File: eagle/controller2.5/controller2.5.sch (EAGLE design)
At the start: 46 parts, among them Q1 MOSFET-PCHANNELNDP6020P_20V_2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, Q2 2N2907, U1 ATMEGA328P

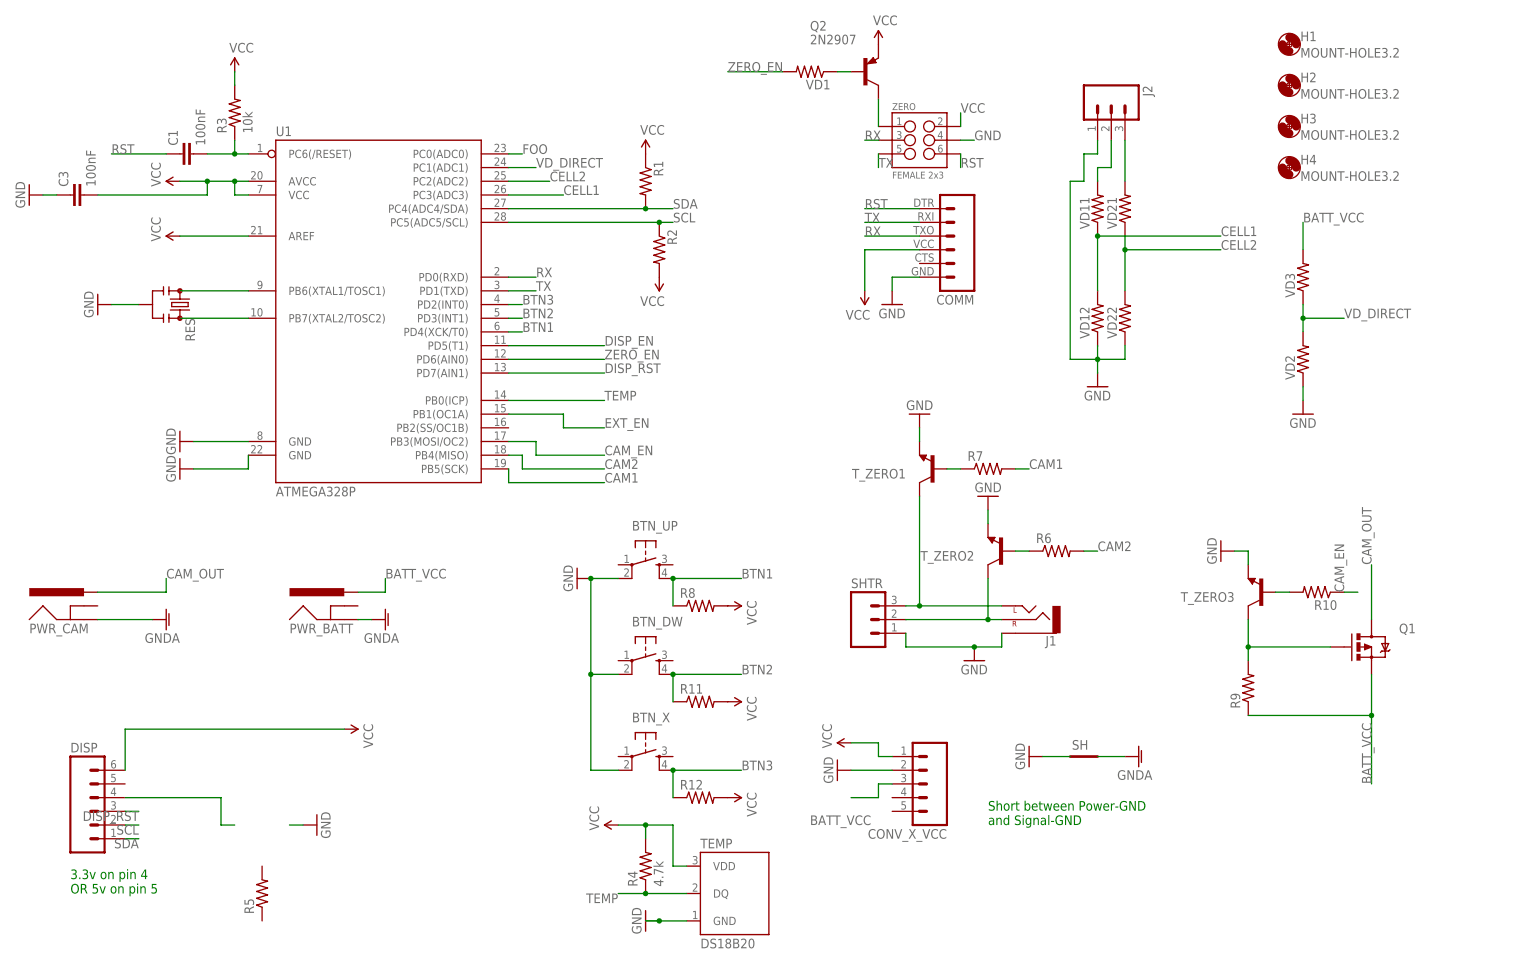
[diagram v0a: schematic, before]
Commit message: controller2.5: smaller board
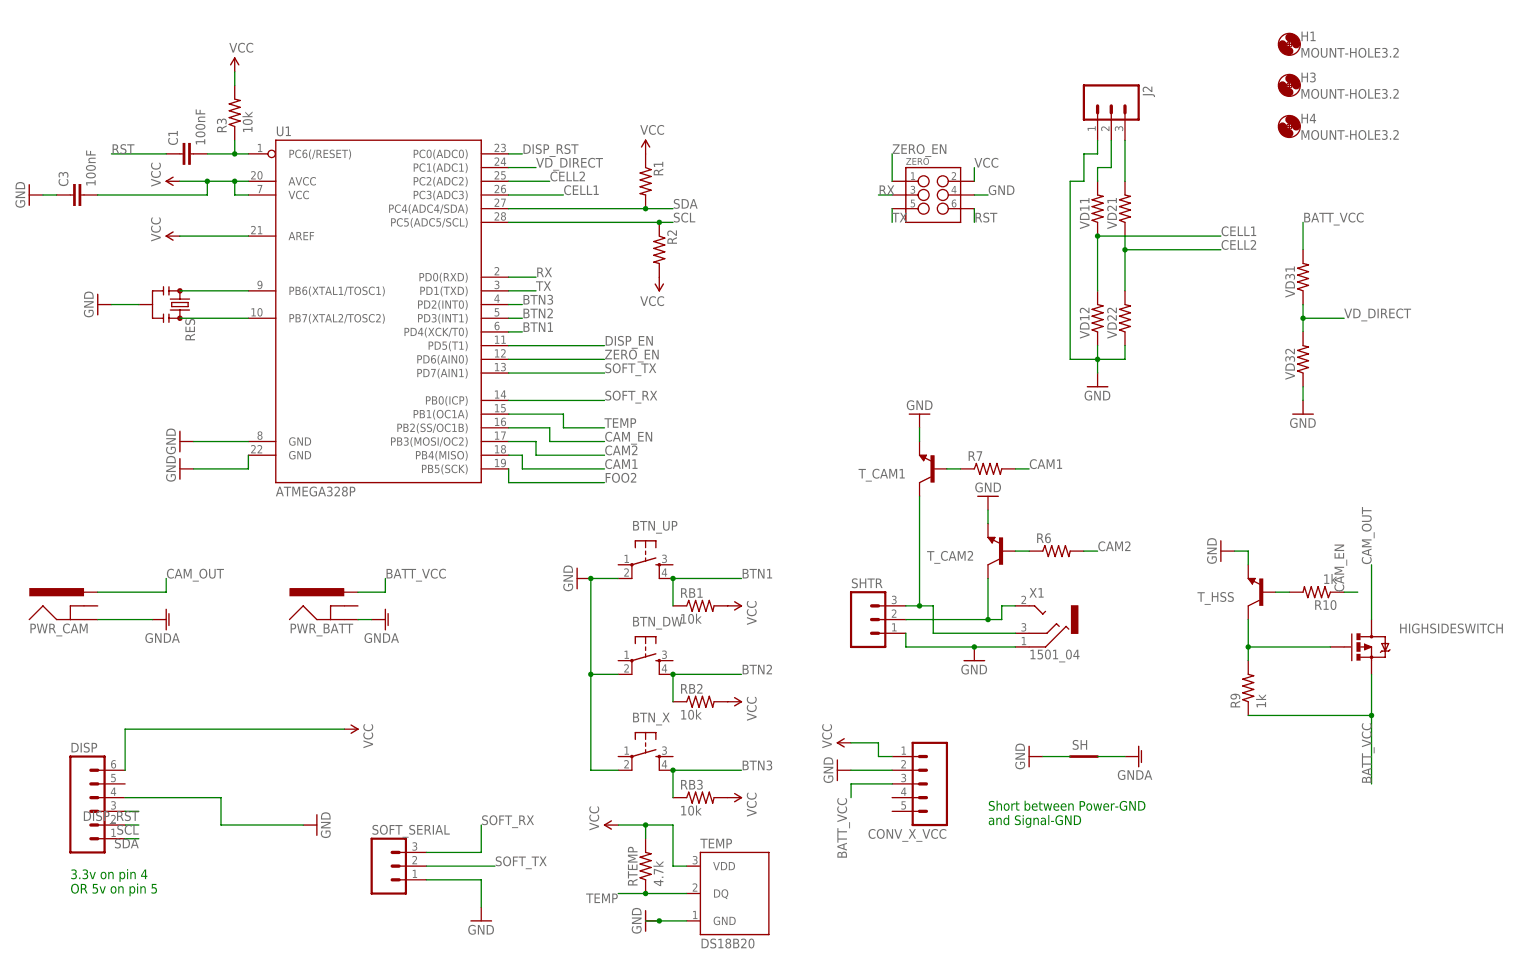
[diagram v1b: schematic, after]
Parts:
- removed COMM: FTDI_BASICPTH, SparkFun-Connectors:FTDI_BASICPTH
- removed H2: MOUNT-HOLE3.2, holes:MOUNT-HOLE3.2
- removed J1: (no value), SparkFun-Connectors:AUDIO-JACK2.5MM
- removed Q2: 2N2907, adafruit:2N2907
- removed R5, VD1: (no value), SparkFun-Resistors:RESISTORAXIAL-0.3
- added SOFT_SERIAL: (no value), SparkFun-Connectors:M03LOCK
- added X1: 1501_04, con-lumberg:1501_04
- R10, R9: value (none) -> 1k
- RB1, RB2, RB3: value (none) -> 10k
- ZERO: value FEMALE 2x3 -> (none)
- renumbered Q1 to HIGHSIDESWITCH, R11 to RB2, R12 to RB3, R4 to RTEMP, R8 to RB1, T_ZERO1 to T_CAM1, T_ZERO2 to T_CAM2, T_ZERO3 to T_HSS, VD2 to VD32, VD3 to VD31
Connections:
- removed net EXT_EN: U1.PB1(OC1A)
- removed net FOO: U1.PC0(ADC0)
- removed net N$12: Q2.C, ZERO.1
- removed net N$4: Q2.B, VD1.1
- removed net N$6: DISP.4
- new net FOO2: U1.PB5(SCK)
- new net SOFT_RX: SOFT_SERIAL.3, U1.PB0(ICP)
- new net SOFT_TX: SOFT_SERIAL.2, U1.PD7(AIN1)
- net CAM1: now also U1.PB4(MISO); no longer U1.PB5(SCK)
- net CAM2: now also U1.PB3(MOSI/OC2); no longer U1.PB4(MISO)
- net CAM_EN: now also U1.PB2(SS/OC1B); no longer U1.PB3(MOSI/OC2)
- net DISP_RST: now also U1.PC0(ADC0); no longer U1.PD7(AIN1)
- net GND: now also DISP.4, SOFT_SERIAL.1, X1.1; no longer COMM.6, J1.SLEEVE
- net N$10: now also X1.3; no longer J1.LEFT
- net N$7: now also X1.2; no longer J1.RIGHT
- net RST: no longer COMM.1
- net RX: no longer COMM.3
- net TEMP: now also U1.PB1(OC1A); no longer U1.PB0(ICP)
- net TX: no longer COMM.2
- net VCC: no longer COMM.4, Q2.E
- net ZERO_EN: now also ZERO.1; no longer VD1.2
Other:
- moved on the sheet: H3, H4, ZERO

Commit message: controller2.5: production version
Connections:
- removed net DISP_EN: U1.PD5(T1)
- removed net FOO2: U1.PB5(SCK)
- net CAM2: now also U1.PB2(SS/OC1B); no longer U1.PB3(MOSI/OC2)
- net CAM_EN: now also U1.PB3(MOSI/OC2); no longer U1.PB2(SS/OC1B)
- net SOFT_TX: now also U1.PB1(OC1A); no longer U1.PD7(AIN1)
- net TEMP: now also U1.PD7(AIN1); no longer U1.PB1(OC1A)
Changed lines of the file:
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@@
 <clearance class="0" value="0.254"/>
 </class>
-<class number="1" name="power" width="0.635" drill="0">
+<class number="1" name="power" width="0.762" drill="0">
 <clearance class="1" value="0.254"/>
 </class>
@@
 </segment>
 <segment>
-<pinref part="U1" gate="G$1" pin="PB3(MOSI/OC2)"/>
-<wire x1="106.68" y1="104.14" x2="111.76" y2="104.14" width="0.1524" layer="91"/>
-<wire x1="111.76" y1="104.14" x2="111.76" y2="101.6" width="0.1524" layer="91"/>
-<wire x1="111.76" y1="101.6" x2="124.46" y2="101.6" width="0.1524" layer="91"/>
-<label x="124.46" y="101.6" size="1.778" layer="95"/>
+<pinref part="U1" gate="G$1" pin="PB2(SS/OC1B)"/>
+<wire x1="106.68" y1="106.68" x2="114.3" y2="106.68" width="0.1524" layer="91"/>
+<wire x1="114.3" y1="106.68" x2="114.3" y2="104.14" width="0.1524" layer="91"/>
+<wire x1="114.3" y1="104.14" x2="124.46" y2="104.14" width="0.1524" layer="91"/>
+<label x="124.46" y="104.14" size="1.778" layer="95"/>
 </segment>
 </net>
@@
 </segment>
 <segment>
-<pinref part="U1" gate="G$1" pin="PB2(SS/OC1B)"/>
-<wire x1="106.68" y1="106.68" x2="114.3" y2="106.68" width="0.1524" layer="91"/>
-<wire x1="114.3" y1="106.68" x2="114.3" y2="104.14" width="0.1524" layer="91"/>
-<wire x1="114.3" y1="104.14" x2="124.46" y2="104.14" width="0.1524" layer="91"/>
-<label x="124.46" y="104.14" size="1.778" layer="95"/>
+<pinref part="U1" gate="G$1" pin="PB3(MOSI/OC2)"/>
+<wire x1="106.68" y1="104.14" x2="111.76" y2="104.14" width="0.1524" layer="91"/>
+<wire x1="111.76" y1="104.14" x2="111.76" y2="101.6" width="0.1524" layer="91"/>
+<wire x1="111.76" y1="101.6" x2="124.46" y2="101.6" width="0.1524" layer="91"/>
+<label x="124.46" y="101.6" size="1.778" layer="95"/>
 </segment>
 </net>
@@
 </segment>
 </net>
-<net name="DISP_EN" class="0">
-<segment>
-<pinref part="U1" gate="G$1" pin="PD5(T1)"/>
-<wire x1="106.68" y1="121.92" x2="124.46" y2="121.92" width="0.1524" layer="91"/>
-<label x="124.46" y="121.92" size="1.778" layer="95"/>
-</segment>
-</net>
 <net name="BTN3" class="0">
 <segment>
@@
 </segment>
 <segment>
-<pinref part="U1" gate="G$1" pin="PB1(OC1A)"/>
-<wire x1="106.68" y1="109.22" x2="116.84" y2="109.22" width="0.1524" layer="91"/>
-<wire x1="116.84" y1="109.22" x2="116.84" y2="106.68" width="0.1524" layer="91"/>
-<wire x1="116.84" y1="106.68" x2="124.46" y2="106.68" width="0.1524" layer="91"/>
-<label x="124.46" y="106.68" size="1.778" layer="95"/>
+<pinref part="U1" gate="G$1" pin="PD7(AIN1)"/>
+<wire x1="106.68" y1="116.84" x2="124.46" y2="116.84" width="0.1524" layer="91"/>
+<label x="124.46" y="116.84" size="1.778" layer="95"/>
 </segment>
 </net>
@@
 </segment>
 </net>
-<net name="FOO2" class="0">
-<segment>
-<pinref part="U1" gate="G$1" pin="PB5(SCK)"/>
-<wire x1="106.68" y1="99.06" x2="106.68" y2="96.52" width="0.1524" layer="91"/>
-<wire x1="106.68" y1="96.52" x2="124.46" y2="96.52" width="0.1524" layer="91"/>
-<label x="124.46" y="96.52" size="1.778" layer="95"/>
-</segment>
-</net>
 <net name="SOFT_TX" class="0">
 <segment>
@@
 </segment>
 <segment>
-<pinref part="U1" gate="G$1" pin="PD7(AIN1)"/>
-<wire x1="106.68" y1="116.84" x2="124.46" y2="116.84" width="0.1524" layer="91"/>
-<label x="124.46" y="116.84" size="1.778" layer="95"/>
-</segment>
-</net>
+<pinref part="U1" gate="G$1" pin="PB1(OC1A)"/>
+<wire x1="106.68" y1="109.22" x2="116.84" y2="109.22" width="0.1524" layer="91"/>
+<wire x1="116.84" y1="109.22" x2="116.84" y2="106.68" width="0.1524" layer="91"/>
+<wire x1="116.84" y1="106.68" x2="124.46" y2="106.68" width="0.1524" layer="91"/>
+<label x="124.46" y="106.68" size="1.778" layer="95"/>
+</segment>
+</net>

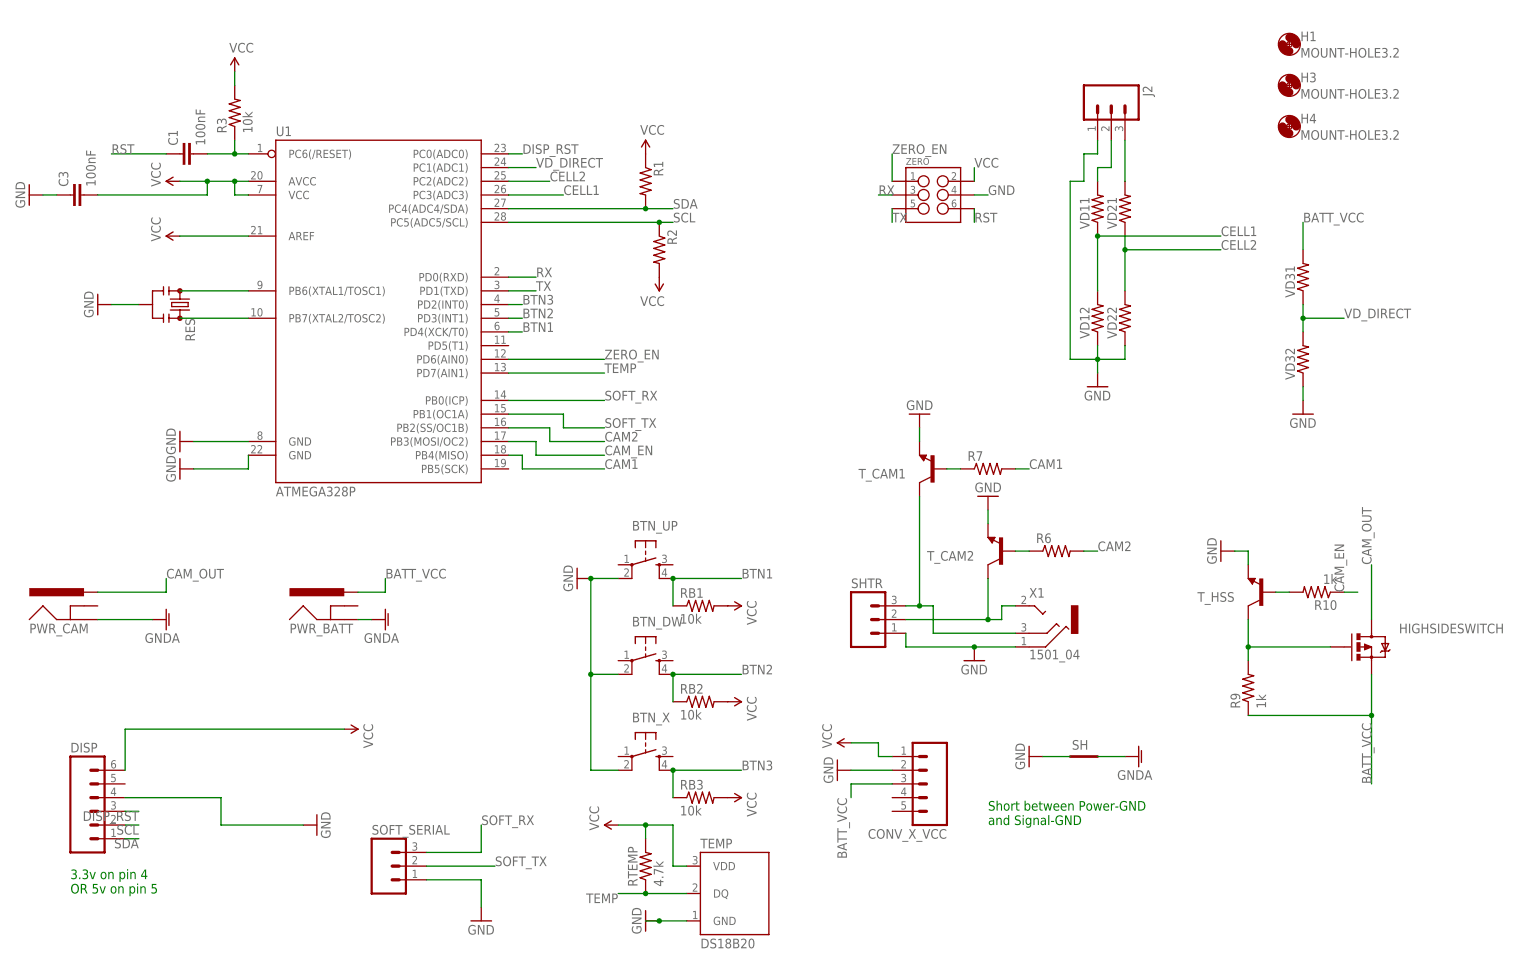
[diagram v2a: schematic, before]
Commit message: small changes in CAD files
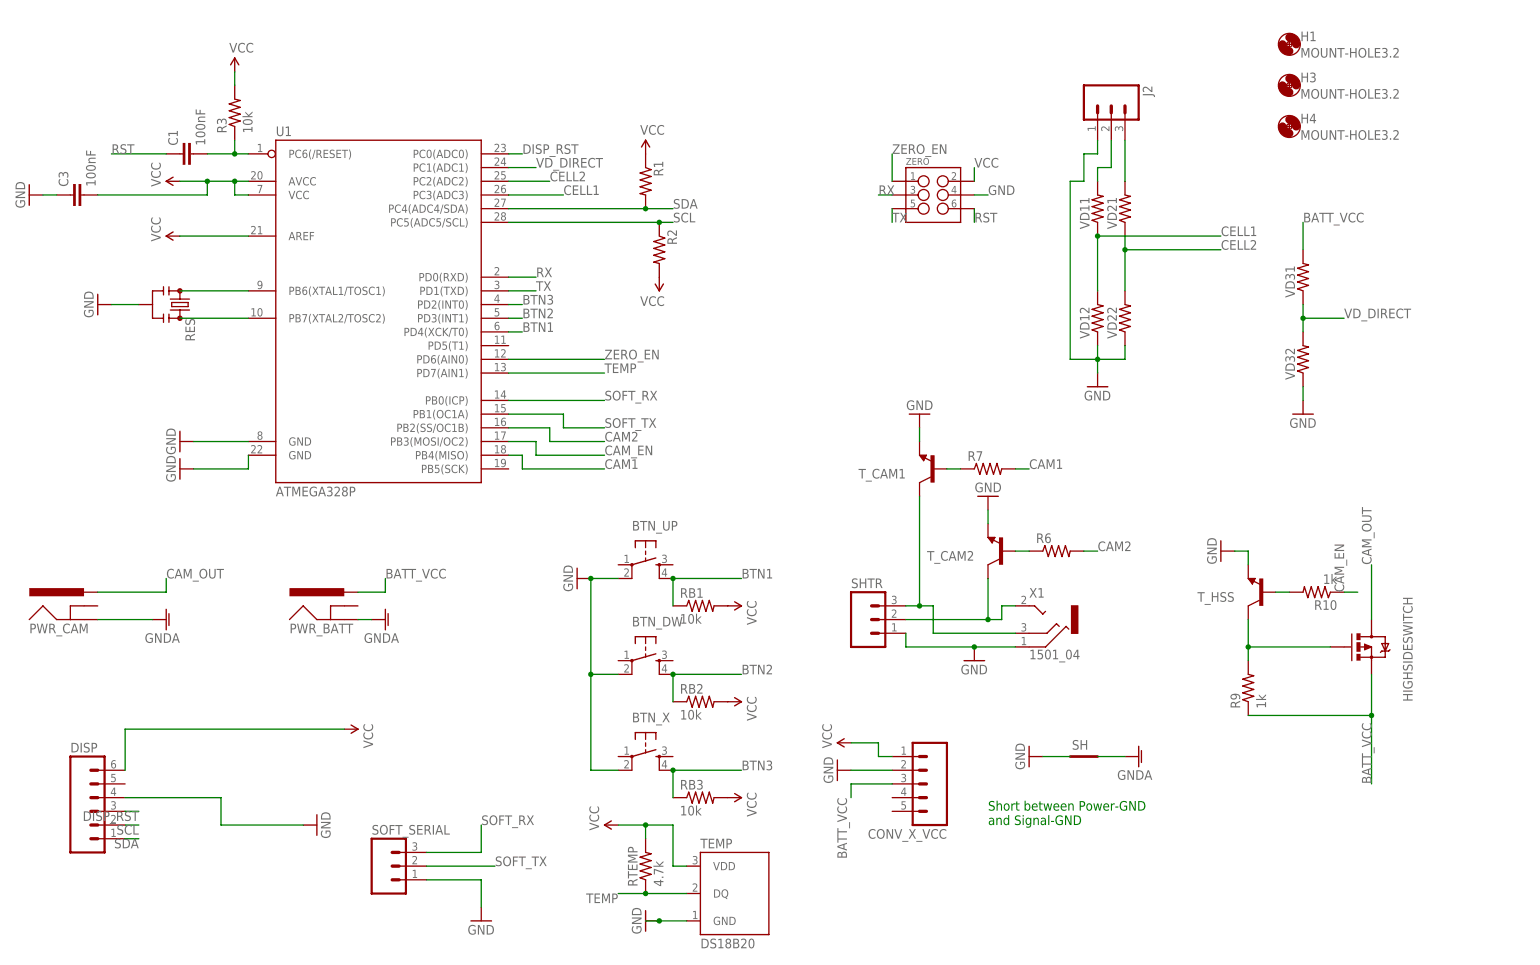
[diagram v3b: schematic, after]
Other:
- note removed: "3.3v on pin 4 OR 5v on pin 5"
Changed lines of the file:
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@@
 <sheet>
 <plain>
-<text x="25.4" y="20.32" size="1.778" layer="91">3.3v on pin 4
-OR 5v on pin 5</text>
 <text x="195.58" y="33.02" size="1.778" layer="91">Short between Power-GND
 and Signal-GND</text>
@@
 <instance part="R6" gate="G$1" x="208.28" y="83.82"/>
 <instance part="R7" gate="G$1" x="195.58" y="99.06"/>
-<instance part="HIGHSIDESWITCH" gate="G$1" x="266.7" y="66.04"/>
+<instance part="HIGHSIDESWITCH" gate="G$1" x="266.7" y="66.04" smashed="yes">
+<attribute name="NAME" x="274.32" y="55.88" size="1.778" layer="95" rot="R90"/>
+<attribute name="VALUE" x="271.78" y="66.04" size="1.778" layer="96"/>
+</instance>
 <instance part="T_HSS" gate="G$1" x="246.38" y="76.2" rot="R180"/>
 <instance part="R9" gate="G$1" x="243.84" y="58.42" rot="R90"/>
